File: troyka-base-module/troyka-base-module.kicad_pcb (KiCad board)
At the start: 2 copper layers, 25.4 x 25.4 mm, 5 parts, among them J1 UP (A), J2 DOWN (A)

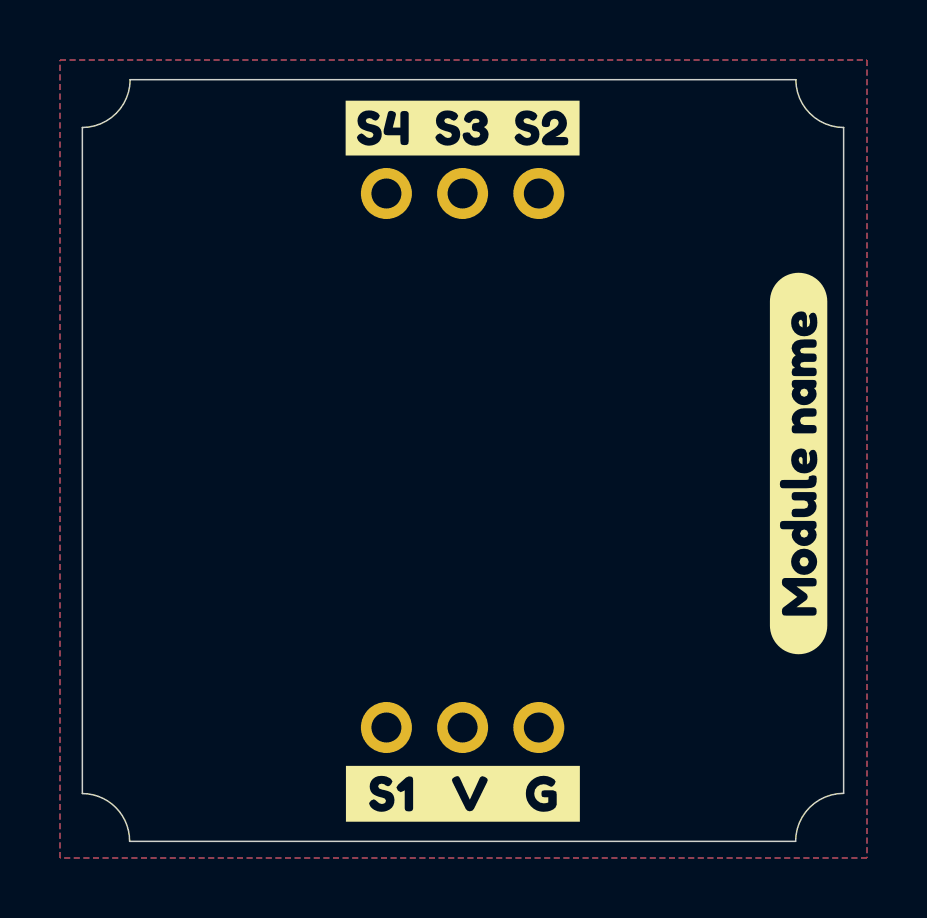
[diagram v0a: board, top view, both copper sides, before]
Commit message: Update templates and CI
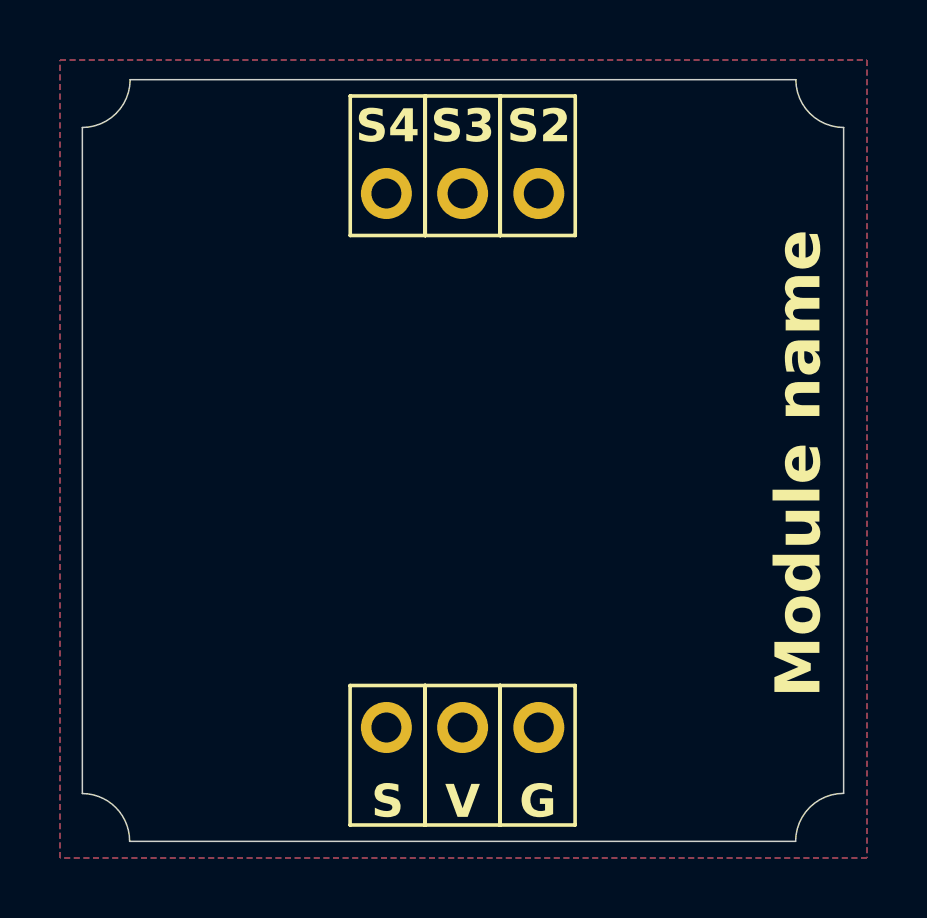
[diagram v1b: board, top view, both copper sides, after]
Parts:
- removed kibuzzard-63E392E0: G***, kibuzzard-63E392E0
- removed kibuzzard-63E39327: G***, kibuzzard-63E39327
- removed kibuzzard-63E393AD: G***, kibuzzard-63E393AD
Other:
- board text added: "G"
- board text added: "Module name"
- board text added: "S"
- board text added: "S2"
- board text added: "S3"
- board text added: "S4"
- board text added: "V"
